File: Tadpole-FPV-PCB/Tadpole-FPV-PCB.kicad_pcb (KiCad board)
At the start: 2 copper layers, 19 parts, among them J1 U1 Debug, J2 U2 Debug, J3 Left Gimbal, J4 Right Gimbal, P1 USB_C_Plug_USB2.0, SW1 Power Switch, SW2 Left Switch, SW3 Right Switch, U1 ESP32-WROOM-32, U2 ESP32-WROOM-32, U3 E28-2G4M27S

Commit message: Finished PCB Schematic Design (Again)
I feel like this might happen a couple more times...
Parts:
- added C2: 22uF, Capacitor_SMD:C_0603_1608Metric, F.Cu at (116.2, 134.4)
- added C3: 22uF, Capacitor_SMD:C_0603_1608Metric, F.Cu at (116.2, 137.0)
- added D2: LED, Diode_SMD:D_0201_0603Metric, F.Cu at (113.7, 129.0)
- added L1: 470nH, Custom:IND-SMD_L4.0-W4.0_XGL4020, F.Cu at (120.9, 135.7)
- added R3: 100, Resistor_SMD:R_0603_1608Metric, F.Cu at (118.4, 127.0)
- added R4: 5.1k, Resistor_SMD:R_0603_1608Metric, F.Cu at (132.2, 126.5)
- added R5: 100k, Resistor_SMD:R_0402_1005Metric, F.Cu at (123.6, 139.3)
- added R6: 511k, Resistor_SMD:R_0402_1005Metric, F.Cu at (123.6, 141.5)
- added R7: 91k, Resistor_SMD:R_0603_1608Metric, F.Cu at (116.2, 139.6)
- R1, R2: footprint Resistor_THT:R_Axial_DIN0207_L6.3mm_D2.5mm_P7.62mm_Horizontal -> Resistor_SMD:R_0603_1608Metric
- U4: footprint Connector_PinHeader_2.54mm:PinHeader_1x04_P2.54mm_Vertical -> Custom:VSON-10_L3.0-W2.0-P0.50-TL
- U5: value (none) -> ~
- moved U4 32.4 mm to (120.3, 140.5)
- moved R1 3.29 mm to (135.2, 106.0)
- moved R2 3.29 mm to (135.2, 110.0)
- turned BT1 to 0 degrees
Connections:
- net Net-(U5-VIN+) renamed VBUS
- BT1 pad 1: Net-(BT1-Pad1) -> GND
- BT2 pad 2: Net-(BT1-Pad1) -> Battery +
- C1 pad 1: +3.3V -> VOUT
- D1 pad 4: +3.3V -> VOUT
- J1 pad 2: +3.3V -> VOUT
- J2 pad 2: +3.3V -> VOUT
- J3 pad 1: +3.3V -> VOUT
- J3 pad 4: +3.3V -> VOUT
- J4 pad 1: +3.3V -> VOUT
- J4 pad 4: +3.3V -> VOUT
- P1 pad A5: unconnected-(P1-CC-PadA5) -> Net-(P1-CC)
- P1 pad B5: unconnected-(P1-VCONN-PadB5) -> Net-(P1-CC)
- R1 pad 2: +3.3V -> VOUT
- R2 pad 2: +3.3V -> VOUT
- SW1 pad 2: Net-(SW1A-B) -> VIN
- SW2 pad 1: unconnected-(SW2A-A-Pad1) -> Left Switch
- SW3 pad 1: unconnected-(SW3A-A-Pad1) -> Right Switch
- U1 pad 10: unconnected-(U1-IO25-Pad10) -> Right Switch
- U1 pad 11: unconnected-(U1-IO26-Pad11) -> Left Switch
- U1 pad 12: unconnected-(U1-IO27-Pad12) -> LED Data
- U1 pad 2: +3.3V -> VOUT
- U1 pad 37: unconnected-(U1-IO23-Pad37) -> SPORT
- U2 pad 2: +3.3V -> VOUT
- U3 pad 1: +3.3V -> VOUT
- U4 pad 1: +3.3V -> VIN
- U4 pad 3: Net-(SW1A-B) -> GND
- U4 pad 4: Net-(SW1A-B) -> FB

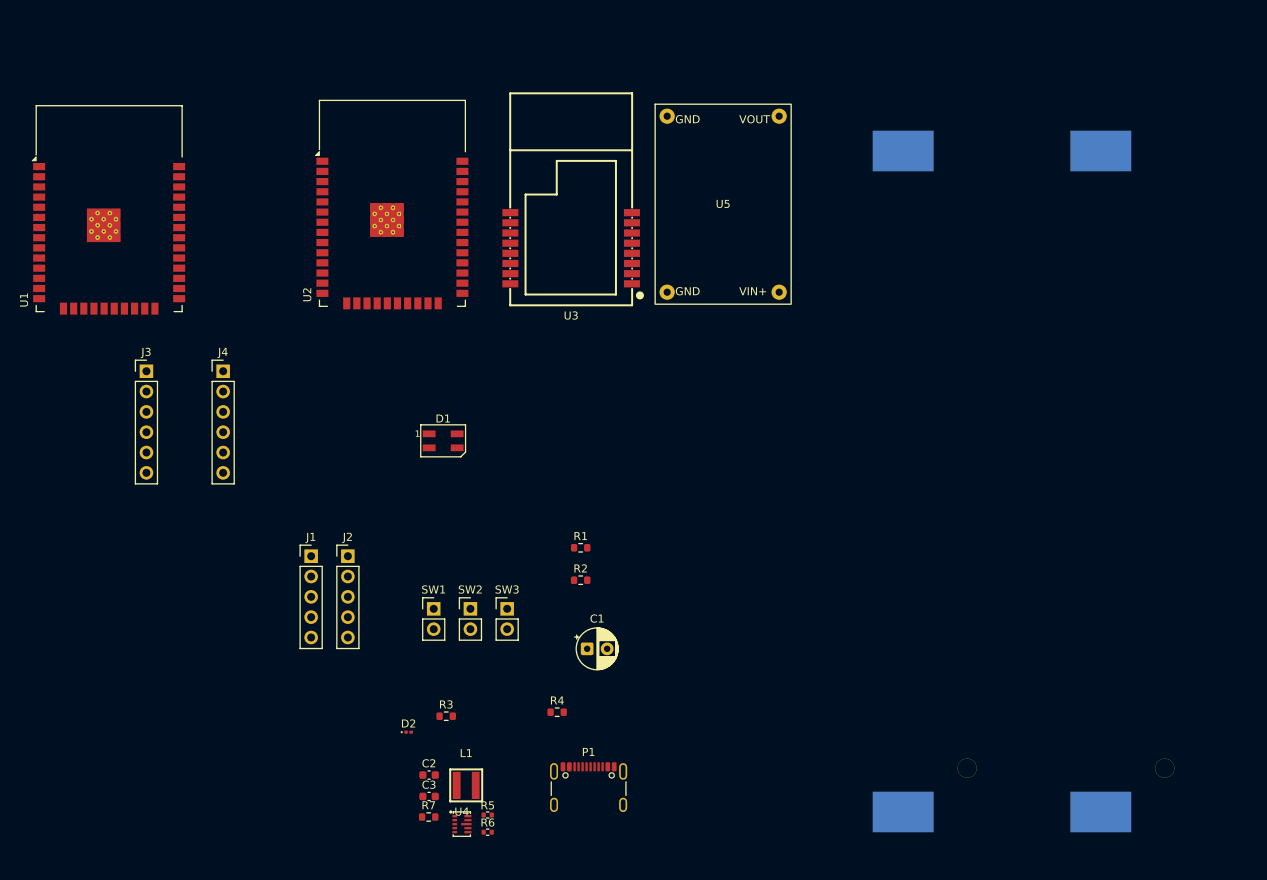
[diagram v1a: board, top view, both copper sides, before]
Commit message: Finished PCB Layout and Wiring + PCB Art!
Also fixed some layout issues from earlier Journal entries.
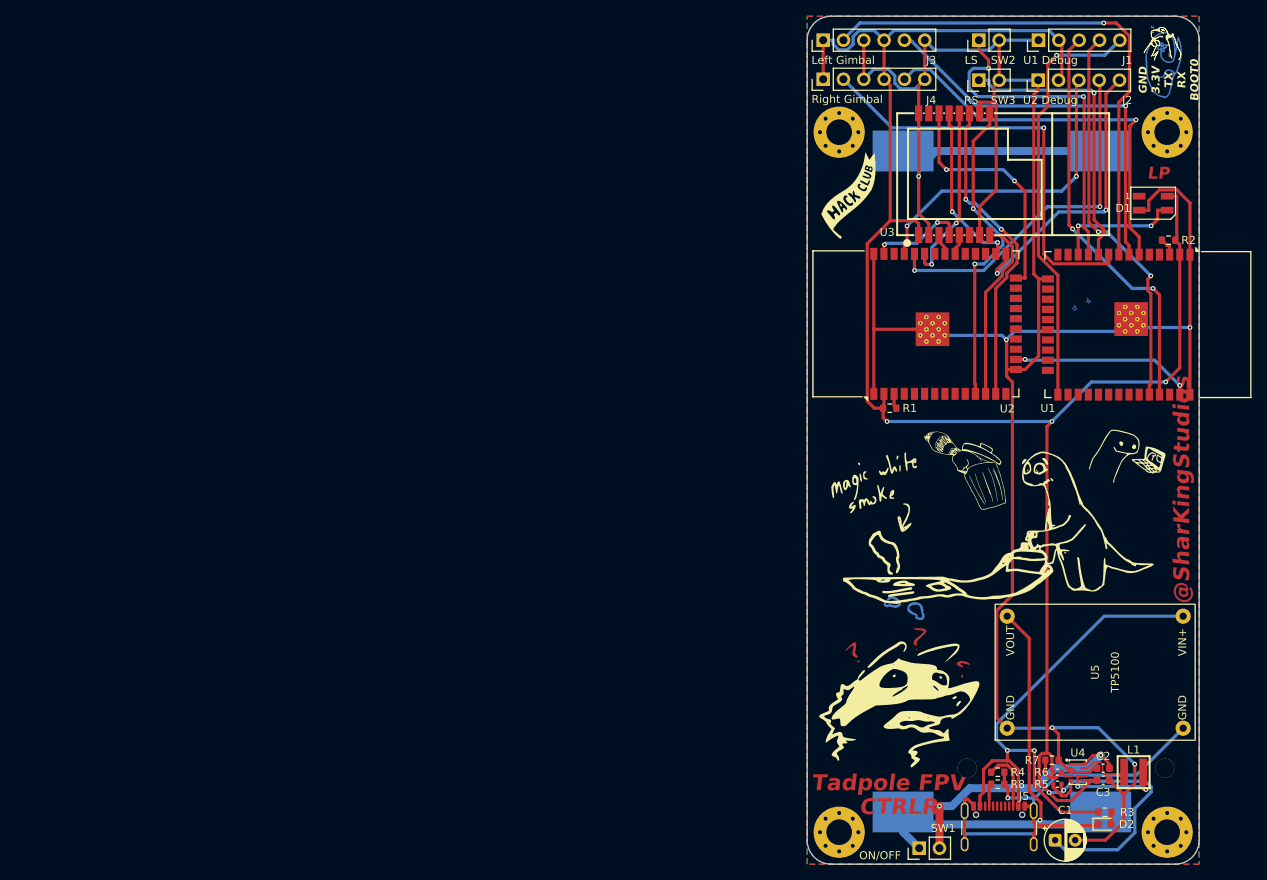
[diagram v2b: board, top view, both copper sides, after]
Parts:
- removed P1: USB_C_Plug_USB2.0, Connector_USB:USB_C_Receptacle_GCT_USB4105-xx-A_16P_TopMnt_Horizontal
- added G***: LOGO, LOGO, F.Cu at (183.0, 96.0)
- added G***: LOGO, LOGO, B.Cu at (200.5, 94.0)
- added G***: LOGO, LOGO, B.Cu at (175.0, 86.0)
- added G***: LOGO, LOGO, B.Cu at (175.2, 99.5)
- added G***: LOGO, LOGO, B.Cu at (175.5, 113.5)
- added G***: LOGO, LOGO, B.Cu at (188.0, 54.0)
- added G***: LOGO, LOGO, B.Cu at (199.5, 111.5)
- added G***: LOGO, LOGO, F.Cu at (166.0, 100.9)
- added G***: LOGO, LOGO, F.Cu at (169.5, 61.5)
- added G***: LOGO, LOGO, F.Cu at (208.0, 43.0)
- added G***: LOGO, LOGO, F.Cu at (174.5, 125.0)
- added G***: LOGO, LOGO, F.Cu at (187.5, 103.0)
- added G***: LOGO, LOGO, F.Cu at (206.2, 97.4)
- added G***: LOGO, LOGO, B.Cu at (199.5, 78.5)
- added G***: LOGO, LOGO, B.Cu at (207.5, 45.5)
- added H1: MountingHole, MountingHole:MountingHole_3.2mm_M3_Pad_Via, F.Cu at (167.5, 141.5)
- added H2: MountingHole, MountingHole:MountingHole_3.2mm_M3_Pad_Via, F.Cu at (167.5, 54.0)
- added H3: MountingHole, MountingHole:MountingHole_3.2mm_M3_Pad_Via, F.Cu at (208.5, 54.0)
- added H4: MountingHole, MountingHole:MountingHole_3.2mm_M3_Pad_Via, F.Cu at (208.5, 141.5)
- added J5: USB_C_Receptacle_USB2.0_16P, Connector_USB:USB_C_Receptacle_GCT_USB4105-xx-A_16P_TopMnt_Horizontal, F.Cu at (187.5, 141.9)
- added R8: 5.1k, Resistor_SMD:R_0603_1608Metric, F.Cu at (187.3, 135.5)
- D2: footprint Diode_SMD:D_0201_0603Metric -> Custom:0603 LED
- SW2: value Left Switch -> LS
- SW3: value Right Switch -> RS
- moved U1 127.4 mm to (203.1, 78.0), turned to -90 degrees
- moved J1 111.5 mm to (192.4, 42.5), turned to 90 degrees
- moved J2 104.8 mm to (192.4, 47.5), turned to 90 degrees
- moved SW2 95.3 mm to (185.0, 42.5), turned to 90 degrees
- moved J3 94.2 mm to (165.5, 42.5), turned to 90 degrees
- moved D1 93.6 mm to (206.8, 62.9)
- moved SW3 88.6 mm to (185.0, 47.5), turned to 90 degrees
- moved D2 87.8 mm to (200.7, 140.6)
- moved R2 84.9 mm to (208.7, 67.5)
- moved C3 84.3 mm to (200.5, 135.0)
- moved C2 84.3 mm to (200.5, 133.5)
- moved L1 83.4 mm to (204.3, 134.0)
- moved J4 83.4 mm to (165.5, 47.4), turned to 90 degrees
- moved R3 83.2 mm to (200.7, 139.0), turned to 180 degrees
- moved R7 78.2 mm to (194.1, 132.5), turned to 180 degrees
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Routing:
- net GND: track 0.00 -> 382.5 mm, vias 0 -> 5
- net VOUT: track 0.00 -> 255.2 mm, vias 0 -> 5
- net VBUS: track 0.00 -> 65.8 mm, vias 0 -> 2
- net Signal 1: track 0.00 -> 65.2 mm, vias 0 -> 1
- net GNDA: track 0.00 -> 62.7 mm, vias 0 -> 1
- net Battery +: track 0.00 -> 59.4 mm, vias 0 -> 1
- net Signal 2: track 0.00 -> 53.1 mm, vias 0 -> 1
- net BOOT 0 U1: track 0.00 -> 53.0 mm, vias 0 -> 1
- net TX U1: track 0.00 -> 51.0 mm, vias 0 -> 2
- net Signal 4: track 0.00 -> 49.8 mm, vias 0 -> 1
- net Signal 3: track 0.00 -> 49.7 mm, vias 0 -> 1
- net RX U1: track 0.00 -> 49.1 mm, vias 0 -> 2
- net RX U2: track 0.00 -> 44.4 mm, vias 0 -> 2
- net Left Switch: track 0.00 -> 43.4 mm, vias 0 -> 2
- net TX_EN U2: track 0.00 -> 39.6 mm, vias 0 -> 2
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- added copper zone on B.Cu, net GND
- added copper zone on F.Cu, net GND
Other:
- board outline added: 49 x 106 mm
- board text added: "3.3V"
- board text added: "@SharKingStudios"
- board text added: "BOOT"
- board text added: "CTRLR"
- board text added: "GND"
- board text added: "GND 3.3V TX RX BOOT0"
- board text added: "LP"
- board text added: "ON/OFF"
- board text added: "RXU1"
- board text added: "RXU2"
- board text added: "SIG1"
- board text added: "SIG2"
- board text added: "SIG3"
- board text added: "SIG4"
- board text added: "TXU1"
- board text added: "TXU2"
- board text added: "Tadpole FPV"
- board text added: "USB-SEE"
